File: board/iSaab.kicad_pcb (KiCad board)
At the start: 2 copper layers, 58.5 x 65.1 mm, 29 parts, among them IC1 MCP2515, IC2 HVD251, IC3 MEGA328, IC4 7805

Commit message: net clean-up
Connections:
- net N$1 renamed TXCAN
- net N$10 renamed STDBY
- net N$12 renamed INT
- net N$14 renamed RESET
- net N$16 renamed XRESET
- net N$2 renamed RXCAN
- net N$31 renamed RX1BF
- net N$4 renamed OSC1
- net N$5 renamed OSC2
- net N$6 renamed TOSC2
- net N$7 renamed TOSC1
- Audio In pad 1: (no net) -> N$17
- Audio In pad 3: (no net) -> N$18
- IC1 pad 11: N$18 -> RX0BF
- R4 pad 2: N$18 -> RX0BF
- R6 pad 2: (no net) -> N$17
- R7 pad 2: (no net) -> N$18
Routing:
- net (no net): track 6.62 -> 0.00 mm
- net RX0BF: track 0.00 -> 5.15 mm
- net N$17: track 0.00 -> 3.62 mm
- net N$18: track 5.15 -> 3.00 mm

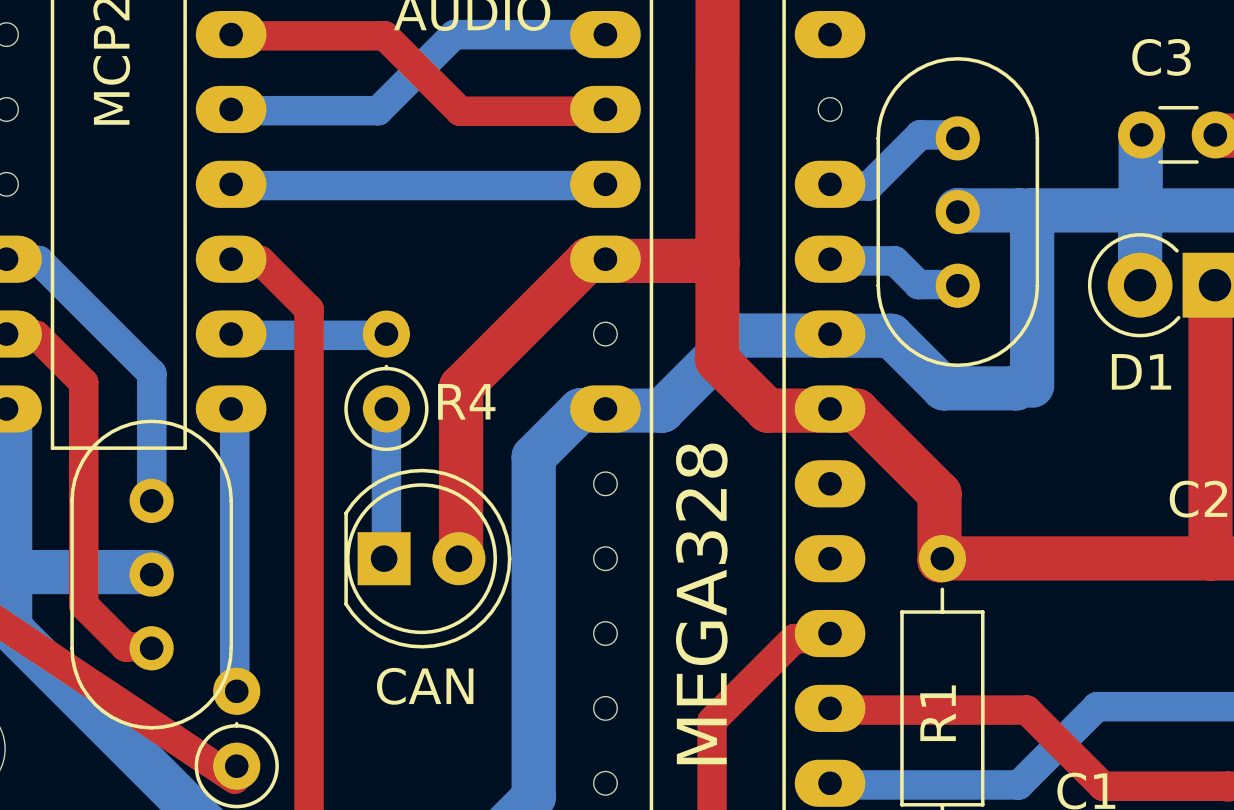
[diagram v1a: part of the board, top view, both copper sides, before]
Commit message: show resonator labels
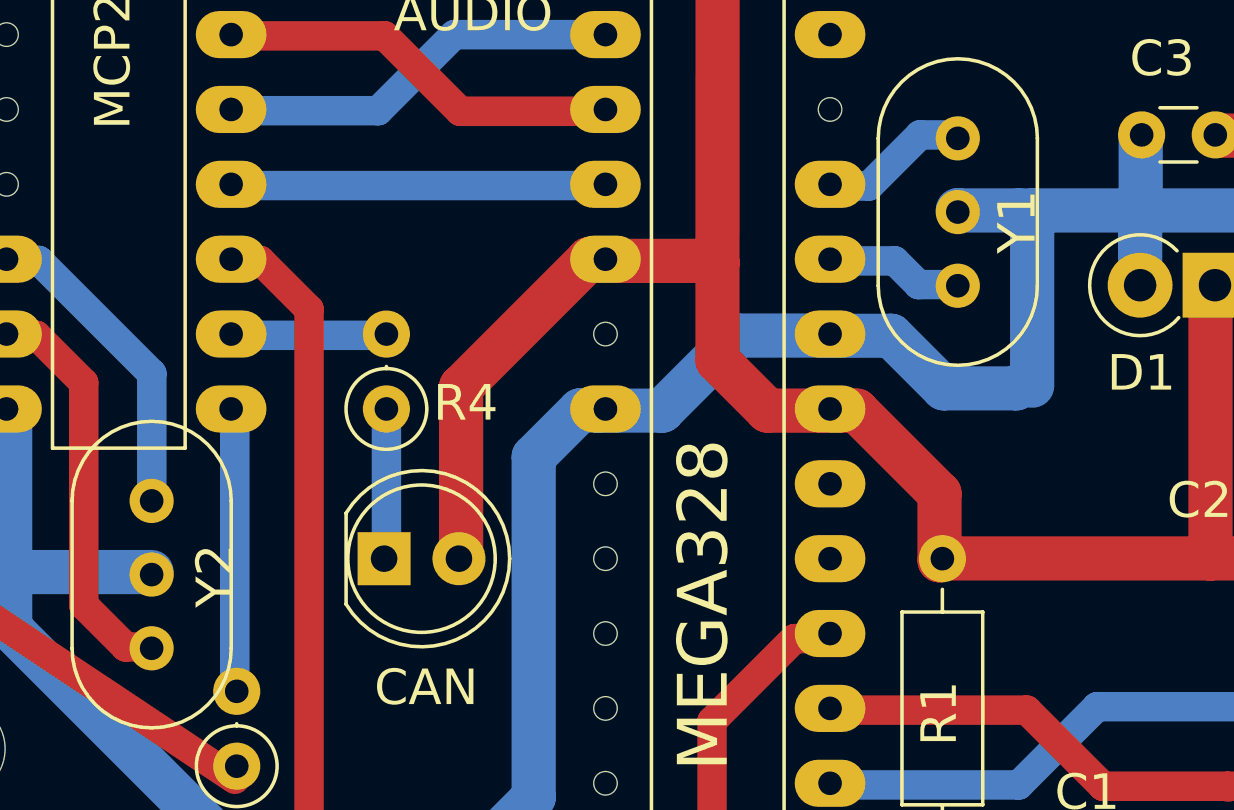
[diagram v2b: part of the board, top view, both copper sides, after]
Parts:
- renumbered U$2 to Y1, U$1 to Y2
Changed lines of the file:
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@@
     (add_net MOSI)
     (add_net N$13)
-    (add_net RESET)
     (add_net N$15)
     (add_net N$17)
     (add_net N$18)
+    (add_net N$35)
     (add_net OSC1)
     (add_net OSC2)
-    (add_net N$35)
+    (add_net RESET)
     (add_net ROUT)
     (add_net RTS)
@@
     (descr "Ceramic Resomator/Filter 10.0x5.0mm^2 RedFrequency MG/MT/MX series, http://www.red-frequency.com/download/datenblatt/redfrequency-datenblatt-ir-zta.pdf, length*width=10.0x5.0mm^2 package, package length=10.0mm, package width=5.0mm, 3 pins")
     (tags "THT ceramic resonator filter")
-    (fp_text reference U$2 (at 2.17 2.016488 90) (layer F.SilkS) hide
+    (fp_text reference Y1 (at 2.17 2.016488 90) (layer F.SilkS)
       (effects (font (size 1.27 1.27) (thickness 0.15)))
     )
@@
     (descr "Ceramic Resomator/Filter 10.0x5.0mm^2 RedFrequency MG/MT/MX series, http://www.red-frequency.com/download/datenblatt/redfrequency-datenblatt-ir-zta.pdf, length*width=10.0x5.0mm^2 package, package length=10.0mm, package width=5.0mm, 3 pins")
     (tags "THT ceramic resonator filter")
-    (fp_text reference U$1 (at 0 -1.426688 270) (layer F.SilkS) hide
+    (fp_text reference Y2 (at 1.452 -1.426688 270) (layer F.SilkS)
       (effects (font (size 1.27 1.27) (thickness 0.15)) (justify right top))
     )

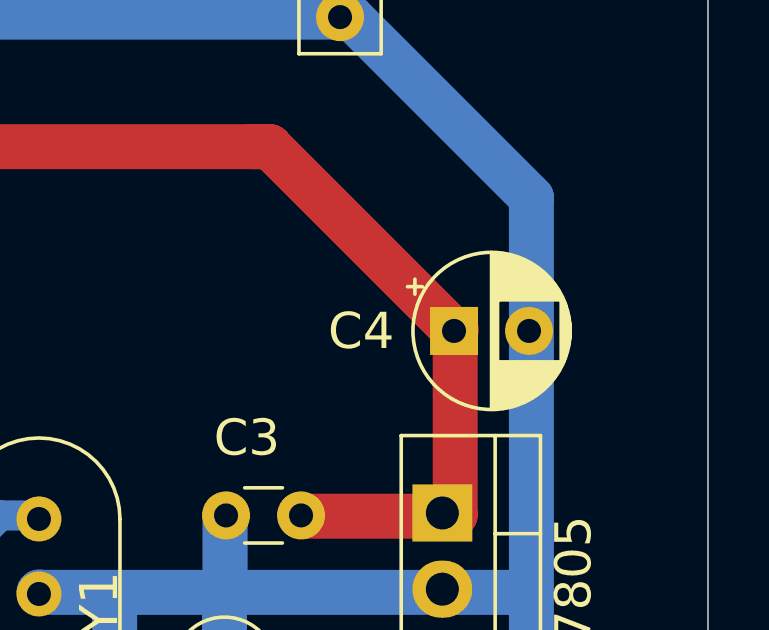
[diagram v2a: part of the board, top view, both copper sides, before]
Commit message: fix skipped track when paused
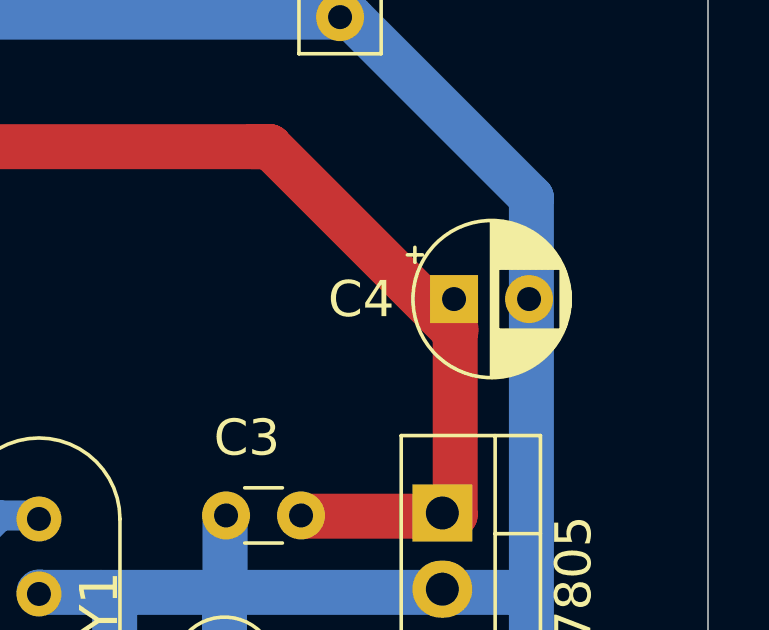
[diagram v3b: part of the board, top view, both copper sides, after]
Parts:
- moved C4 1.06 mm to (169.3, 102.9)
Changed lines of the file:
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@@
   )
   (module Capacitor_THT:CP_Radial_D5.0mm_P2.50mm (layer Top)
-    (at 169.3 103.932173)
+    (at 169.3 102.87)
     (descr "CP, Radial series, Radial, pin pitch=2.50mm, , diameter=5mm, Electrolytic Capacitor")
     (tags "CP Radial series Radial pin pitch 2.50mm  diameter 5mm Electrolytic Capacitor")
